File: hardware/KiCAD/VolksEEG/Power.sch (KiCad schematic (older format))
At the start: 37 parts, among them U4 LM2660MX, U5 TPS78425Q, U6 TPS72325Q

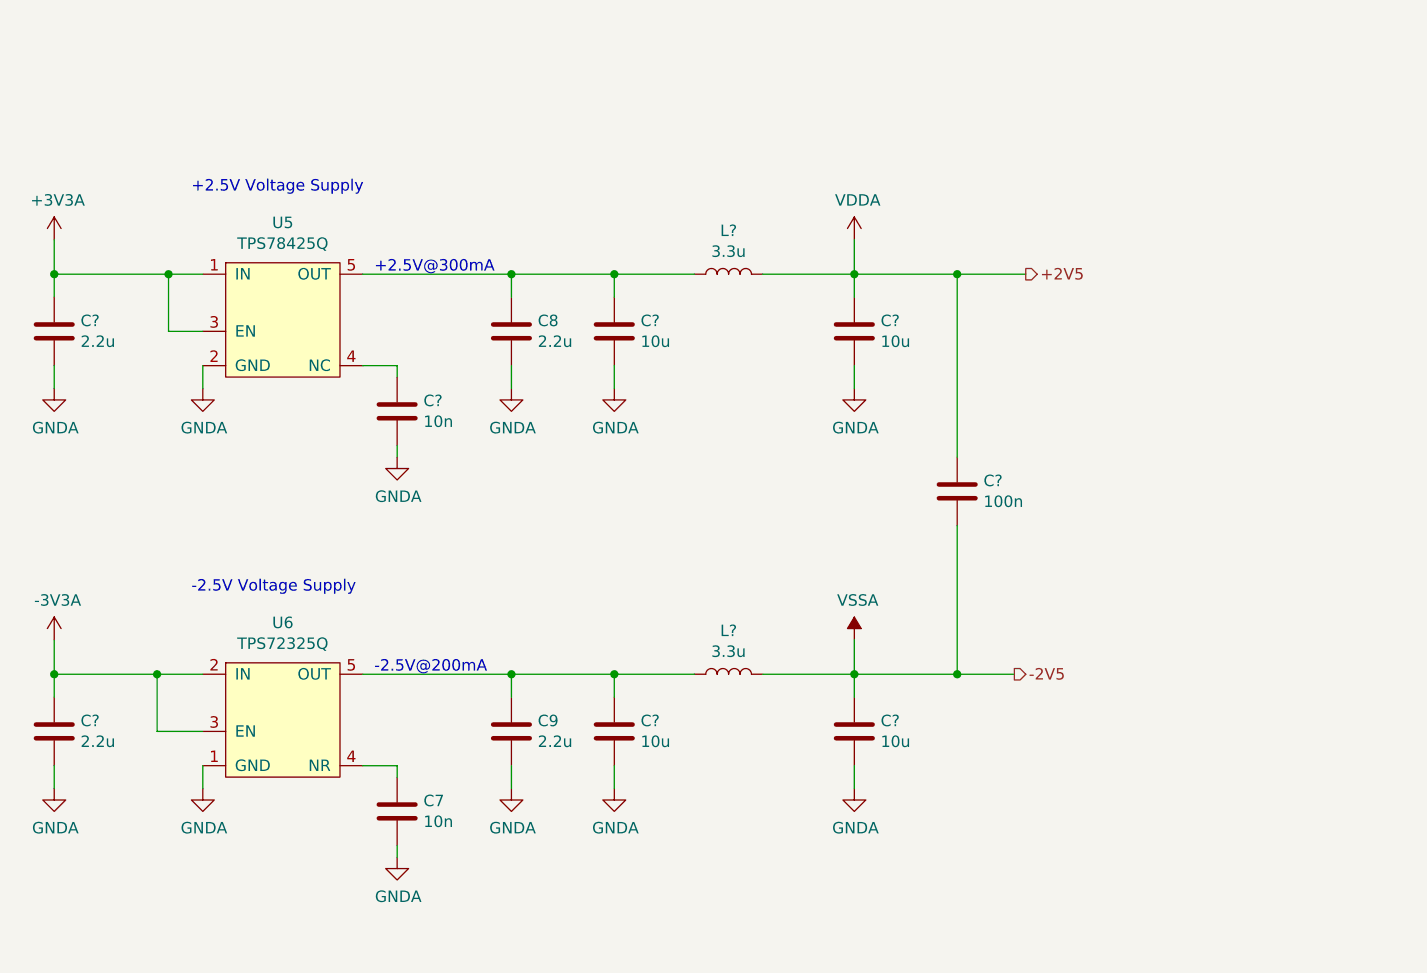
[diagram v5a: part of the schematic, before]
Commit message: Changed -2.5V Regulator due to part availability.
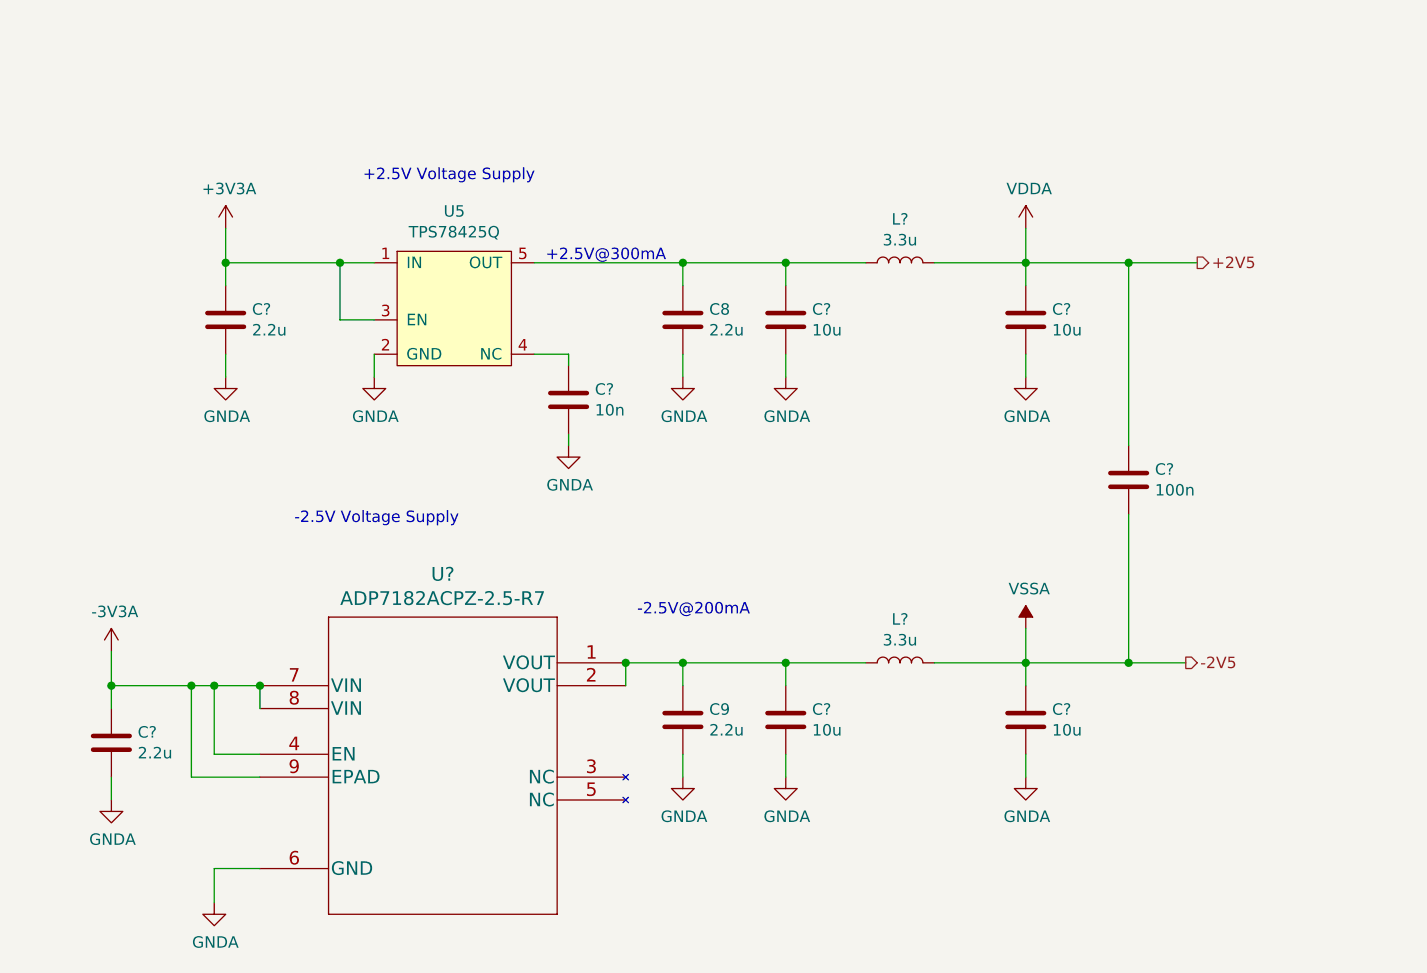
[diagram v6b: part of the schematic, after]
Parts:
- removed C7: 10n, Capacitor_SMD:C_0603_1608Metric_Pad1.08x0.95mm_HandSolder, symbol Device:C
- removed U6: TPS72325Q, VolksEEG:SOT95P280X145-5N, symbol VolksEEG:TPS72325Q
- added U?: ADP7182ACPZ-2.5-R7, CP_8_11_ADI, symbol VolksEEG:ADP7182ACPZ-2.5-R7
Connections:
- net +3V3: now also U?.4 (EN), U?.7 (VIN), U?.8 (VIN), U?.9 (EPAD)
- net GNDA: now also U?.6 (GND)
- net at C9.1, C?.1, L?.1: now also U?.1 (VOUT), U?.2 (VOUT)
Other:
- moved on the sheet: C8, C9, C?, L?, U5

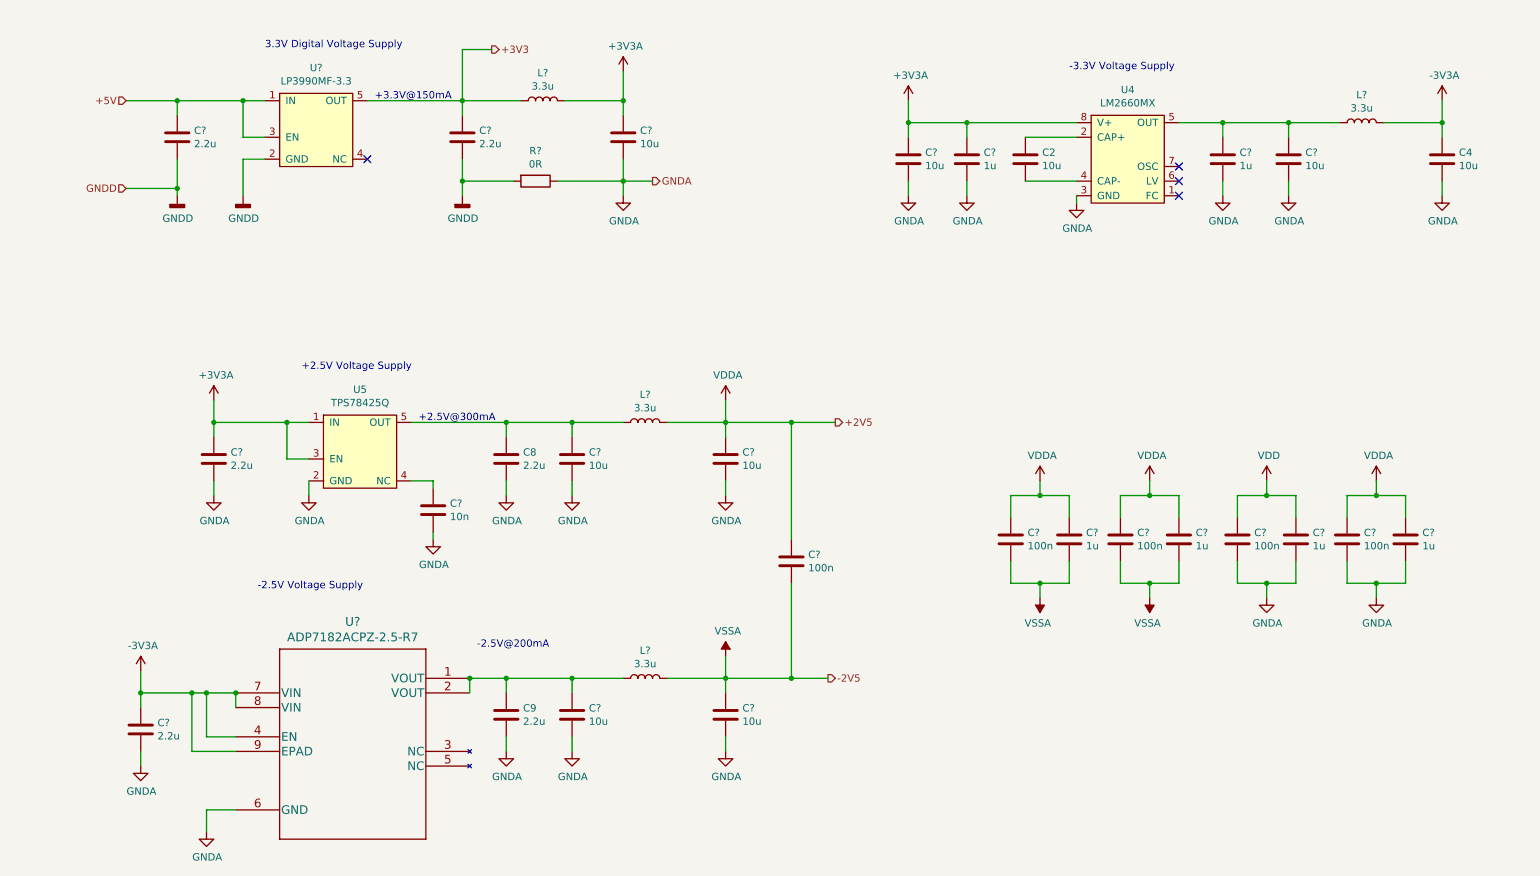
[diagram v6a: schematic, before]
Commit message: Added debugging bits to more schematic sheets.
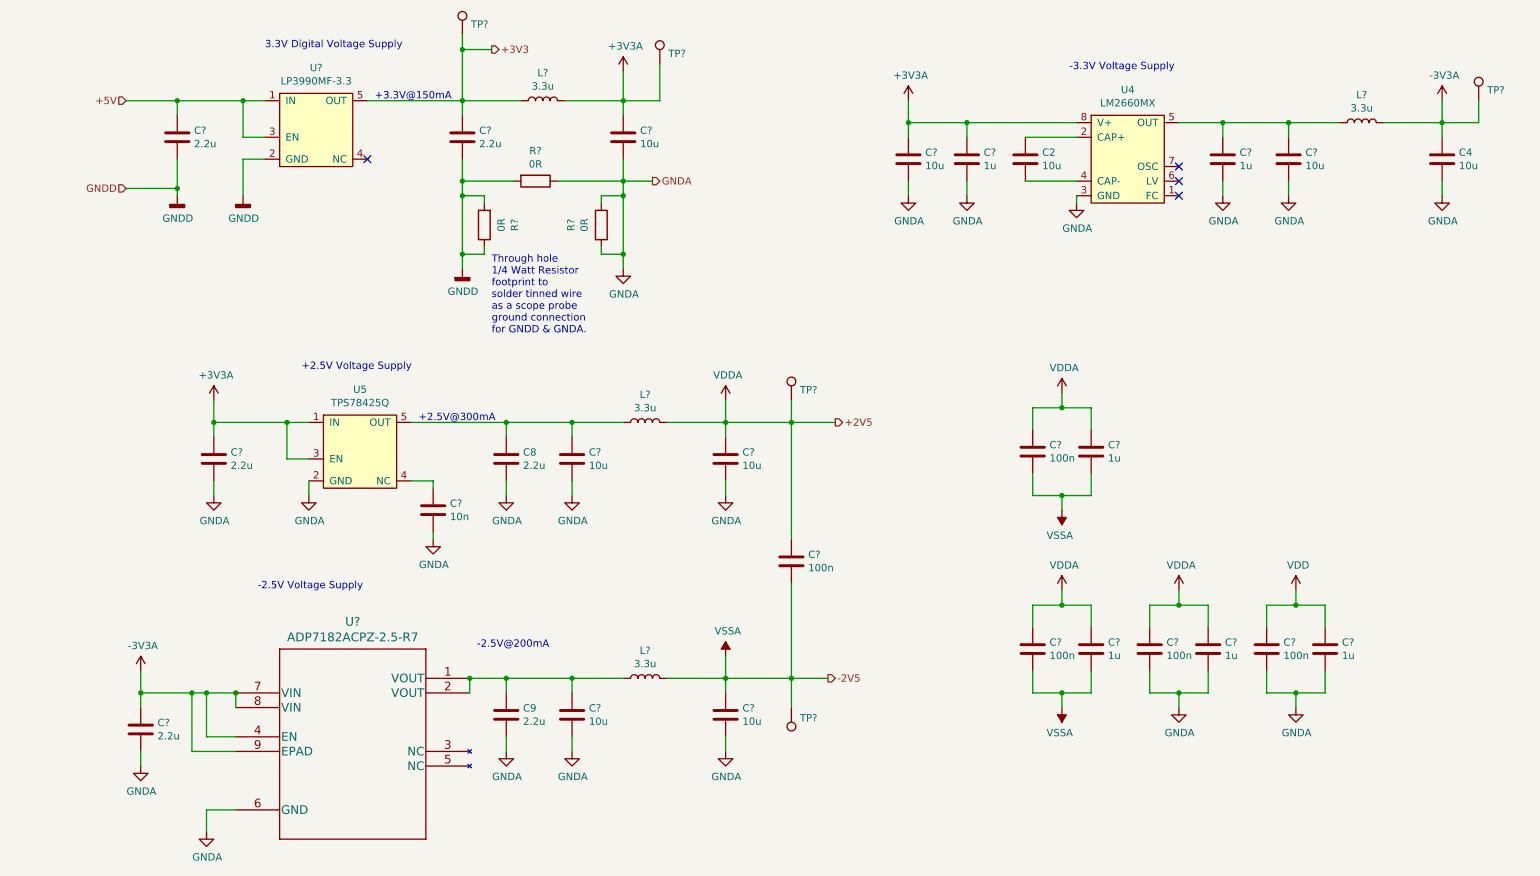
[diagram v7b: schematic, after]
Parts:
- added R? (x2): 0R, symbol Device:R
- added TP?: VDD_+3V3, symbol Connector:TestPoint
- added TP?: +3V3A, symbol Connector:TestPoint
- added TP?: -3V3A, symbol Connector:TestPoint
- added TP?: +2V5, symbol Connector:TestPoint
- added TP?: -2V5, symbol Connector:TestPoint
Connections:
- net +3V3: now also TP?.1, TP?.1, TP?.1
- net GNDA: now also R?.1, R?.2
- net GNDD: now also R?.1, R?.2
- net VDDA: now also TP?.1
- net VSSA: now also TP?.1
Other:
- note added: "Through hole \n1/4 Watt Resistor \nfootprint to \nsolder tinned wire \nas a scope probe \nground connection\nfor GNDD & GNDA."
- moved on the sheet: C?

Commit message: finished off tasks list.
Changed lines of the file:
@@
 Wire Wire Line
 	1850 1900 1850 1950
-Text HLabel 5100 1850 2    50   Output ~ 0
+Text HLabel 5250 1850 2    50   Output ~ 0
 GNDA
 Wire Wire Line
-	4900 1850 5100 1850
+	4900 1850 5250 1850
 $Comp
 L power:GNDD #PWR?
@@
 Wire Wire Line
 	3800 1950 3800 1850
+Text HLabel 5250 1300 2    50   Output ~ 0
++3V3A
+Wire Wire Line
+	5150 1300 5250 1300
+Connection ~ 5150 1300
 $EndSCHEMATC
